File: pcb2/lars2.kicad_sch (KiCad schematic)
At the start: 1 part, among them U1 Pico

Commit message: add 3d model to prototype pcb
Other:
- title: (none) -> LARS V2
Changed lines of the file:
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@@
 	(generator_version "8.0")
 	(paper "A4")
+	(title_block
+		(title "LARS V2")
+		(date "2024-04-01")
+		(rev "1")
+		(comment 1 "https://git.xythobuz.de/thomas/drumkit")
+		(comment 2 "Licensed under the CERN-OHL-S-2.0+")
+		(comment 4 "Copyright (c) 2024 Kauzerei, Thomas Buck")
+	)
 	(symbol
 		(lib_id "KiCad-RP-Pico:Pico")

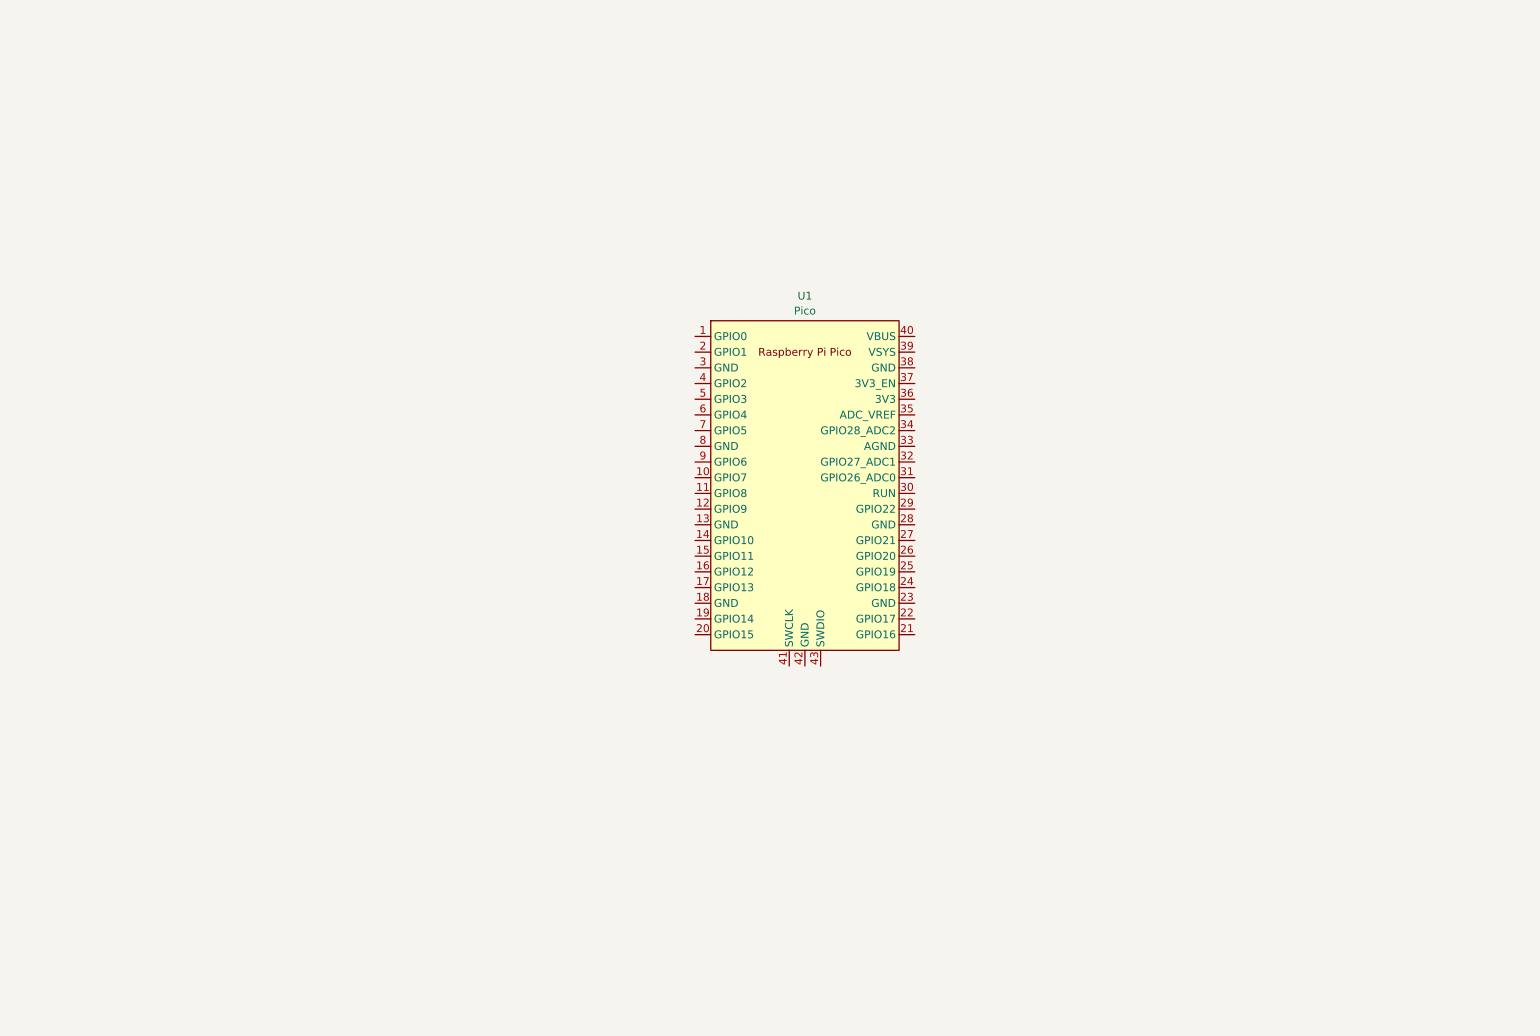
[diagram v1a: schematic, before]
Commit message: add more parts to pcb2
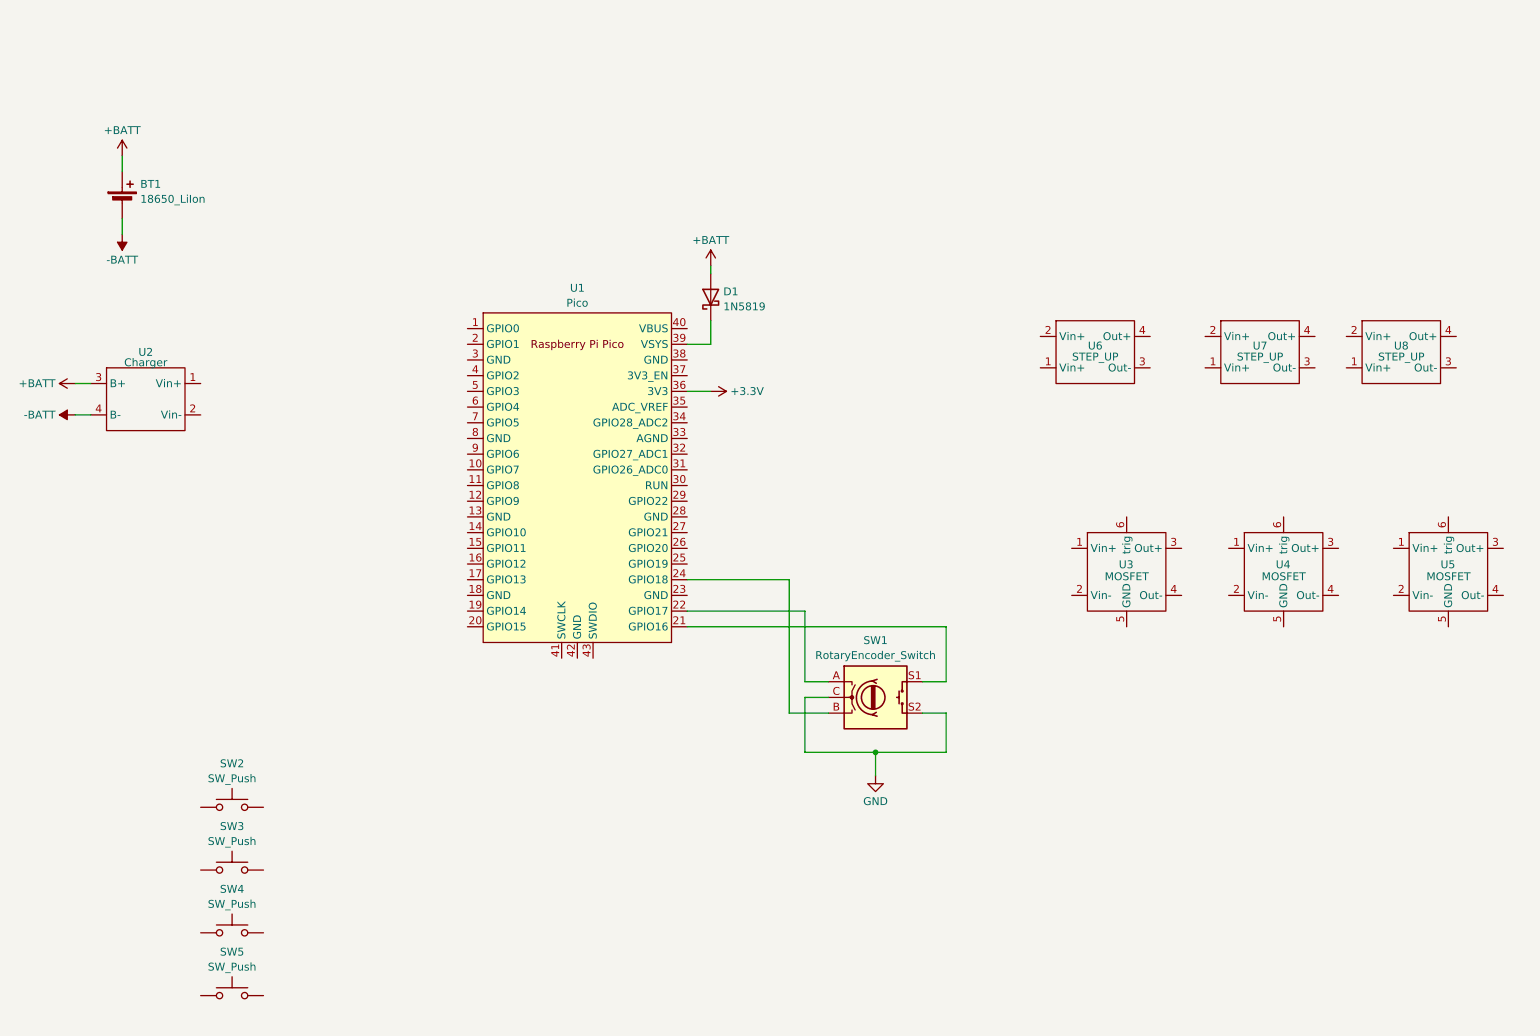
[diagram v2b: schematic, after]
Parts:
- added BT1: 18650_LiIon, Battery:BatteryHolder_Keystone_1042_1x18650, symbol Device:Battery_Cell
- added D1: 1N5819, Diode_THT:D_DO-41_SOD81_P10.16mm_Horizontal, symbol Diode:1N5819
- added SW1: RotaryEncoder_Switch, Rotary_Encoder:RotaryEncoder_Alps_EC12E-Switch_Vertical_H20mm_CircularMountingHoles, symbol Device:RotaryEncoder_Switch
- added SW2, SW3, SW4, SW5: SW_Push, Button_Switch_THT:SW_PUSH_6mm_H5mm, symbol Switch:SW_Push
- added U2: Charger, chinese_modules:charger, symbol chinese_modules:charger
- added U3, U4, U5: MOSFET, chinese_modules:xy-mos, symbol chinese_modules:xy-mos
- added U6, U7, U8: STEP_UP, chinese_modules:dc-dc module, symbol chinese_modules:dc-dc
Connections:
- net at U1.21 (GPIO16): now also SW1.S1
- net at U1.22 (GPIO17): now also SW1.A
- net at U1.24 (GPIO18): now also SW1.B
- net +3.3V: now reaches U1.36 (3V3)
- net at U1.39 (VSYS): now also D1.1 (K)
- new net +BATT: BT1.1 (+), D1.2 (A), U2.3 (B+)
- new net -BATT: BT1.2 (-), U2.4 (B-)
- new net GND: SW1.C, SW1.S2
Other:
- moved on the sheet: U1

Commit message: add more parts for pcb2 and work on placement
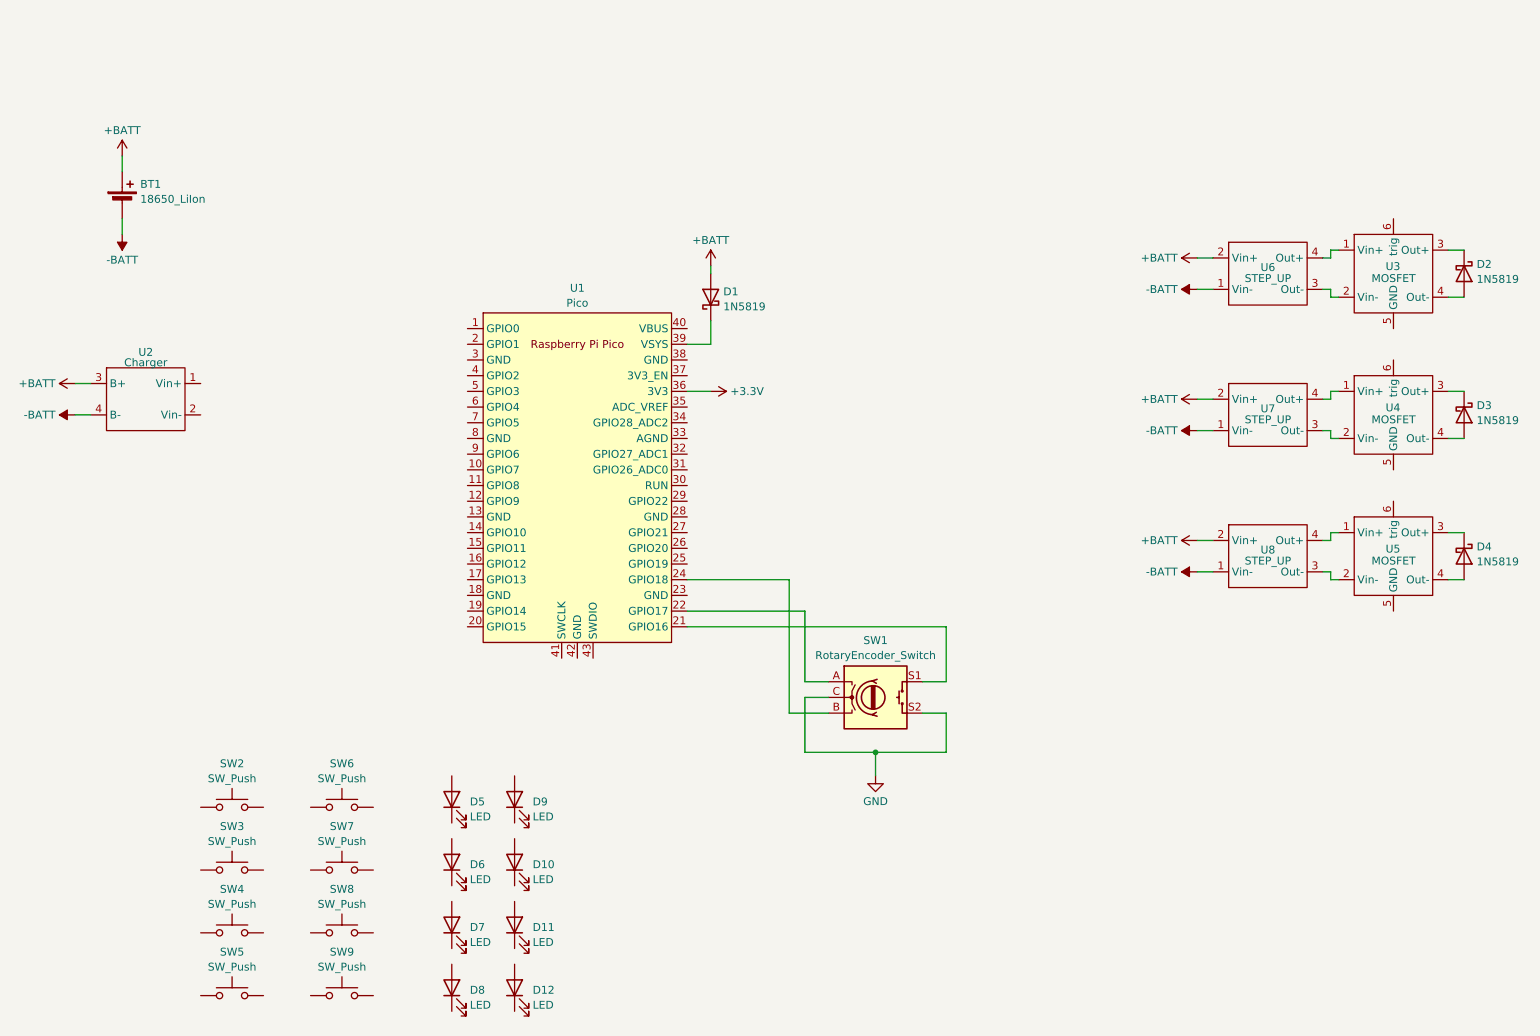
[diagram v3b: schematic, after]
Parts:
- added D10, D11, D12, D5, D6, D7, D8, D9: LED, LED_THT:LED_D5.0mm, symbol Device:LED
- added D2, D3, D4: 1N5819, Diode_THT:D_DO-41_SOD81_P10.16mm_Horizontal, symbol Diode:1N5819
- added SW6, SW7, SW8, SW9: SW_Push, Button_Switch_THT:SW_PUSH_6mm_H5mm, symbol Switch:SW_Push
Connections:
- net +BATT: now also U6.2 (Vin+), U7.2 (Vin+), U8.2 (Vin+)
- net -BATT: now also U6.1 (Vin-), U7.1 (Vin-), U8.1 (Vin-)
- net at U3.1 (Vin+): now also U6.4 (Out+)
- net at U3.2 (Vin-): now also U6.3 (Out-)
- net at U3.3 (Out+): now also D2.1 (K)
- net at U3.4 (Out-): now also D2.2 (A)
- net at U8.3 (Out-): now also U5.2 (Vin-)
- net at U8.4 (Out+): now also U5.1 (Vin+)
- net at U4.1 (Vin+): now also U7.4 (Out+)
- net at U4.2 (Vin-): now also U7.3 (Out-)
- net at U4.3 (Out+): now also D3.1 (K)
- net at U4.4 (Out-): now also D3.2 (A)
- net at U5.3 (Out+): now also D4.1 (K)
- net at U5.4 (Out-): now also D4.2 (A)
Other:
- moved on the sheet: U3, U4, U5, U6, U7, U8

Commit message: add ssd1306 oled to pcb2
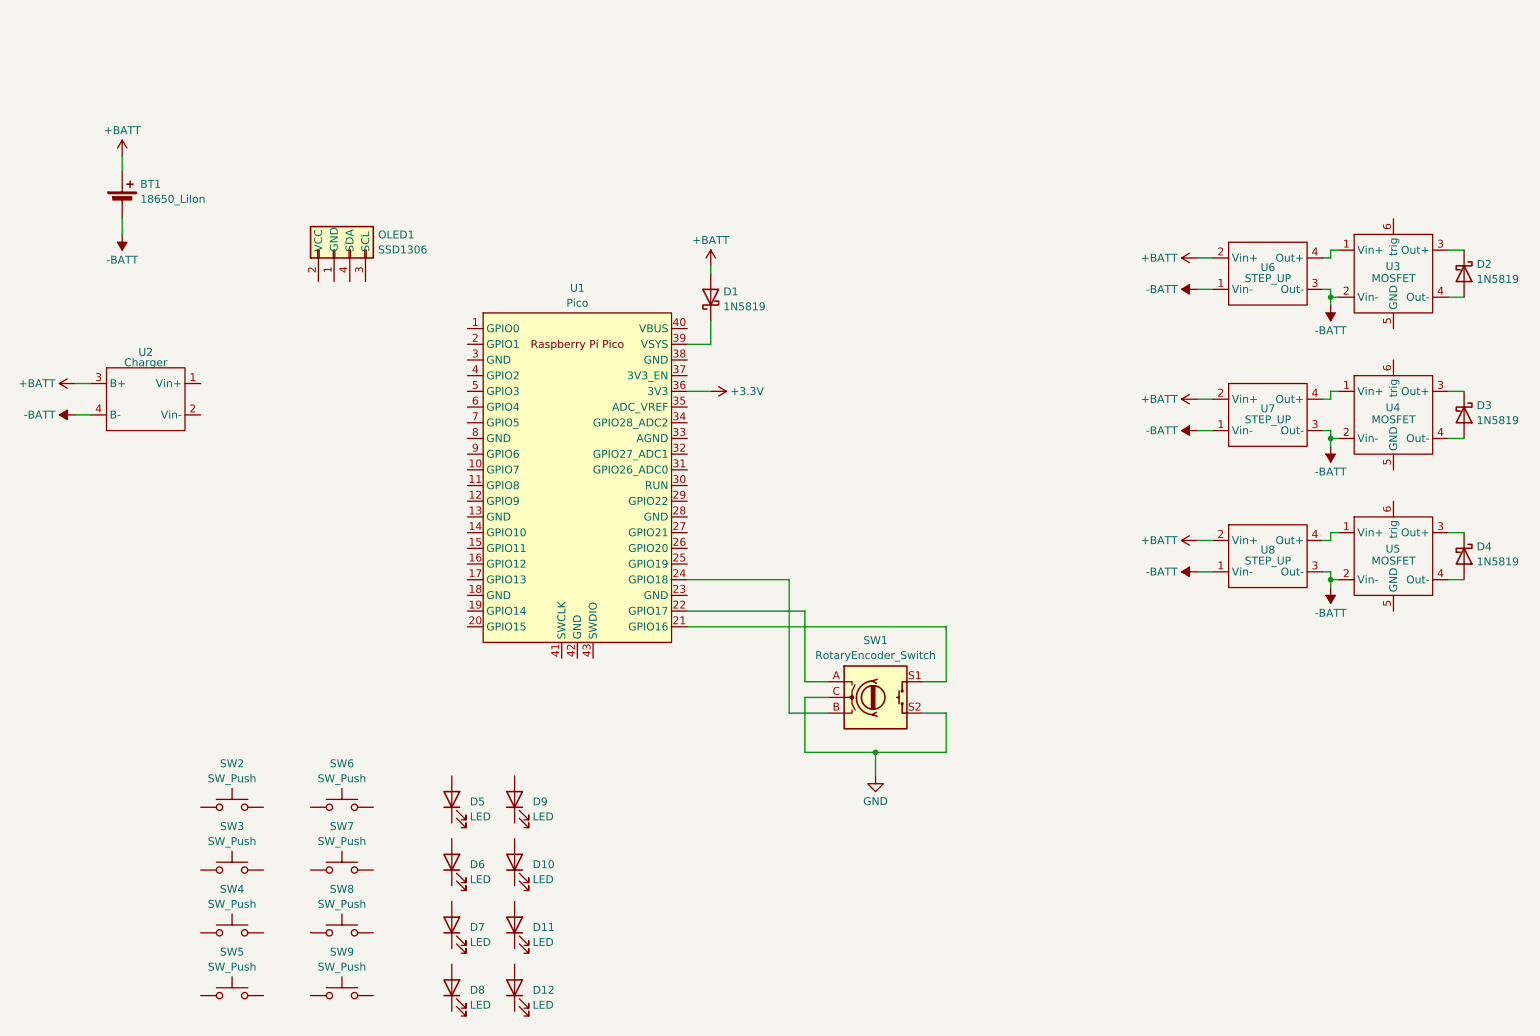
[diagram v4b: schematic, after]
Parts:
- added OLED1: SSD1306, ssd1306:SSD1306_0.96_Oled, symbol ssd1306:SSD1306
- U1: footprint MCU_RaspberryPi_and_Boards:RPi_Pico_SMD_TH -> KiCad-RP-Pico:RPi_Pico_SMD_only
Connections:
- net -BATT: now also U3.2 (Vin-), U4.2 (Vin-), U5.2 (Vin-), U6.3 (Out-), U7.3 (Out-), U8.3 (Out-)

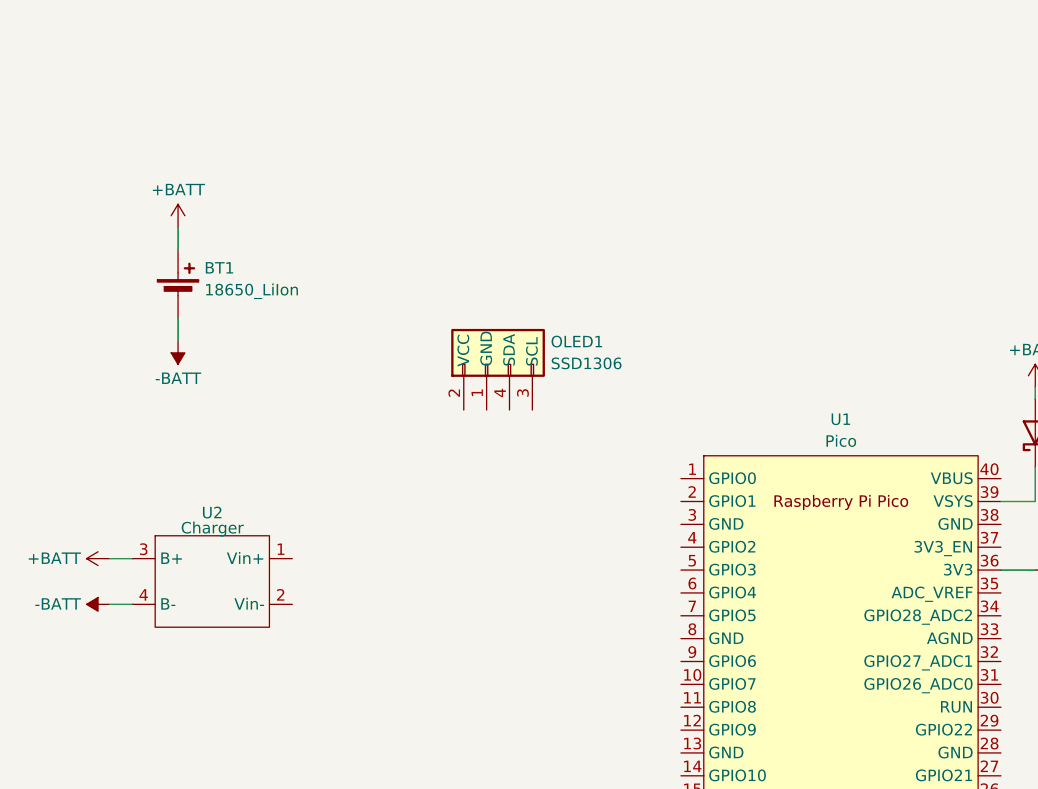
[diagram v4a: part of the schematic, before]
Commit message: add power switch and finish output routing
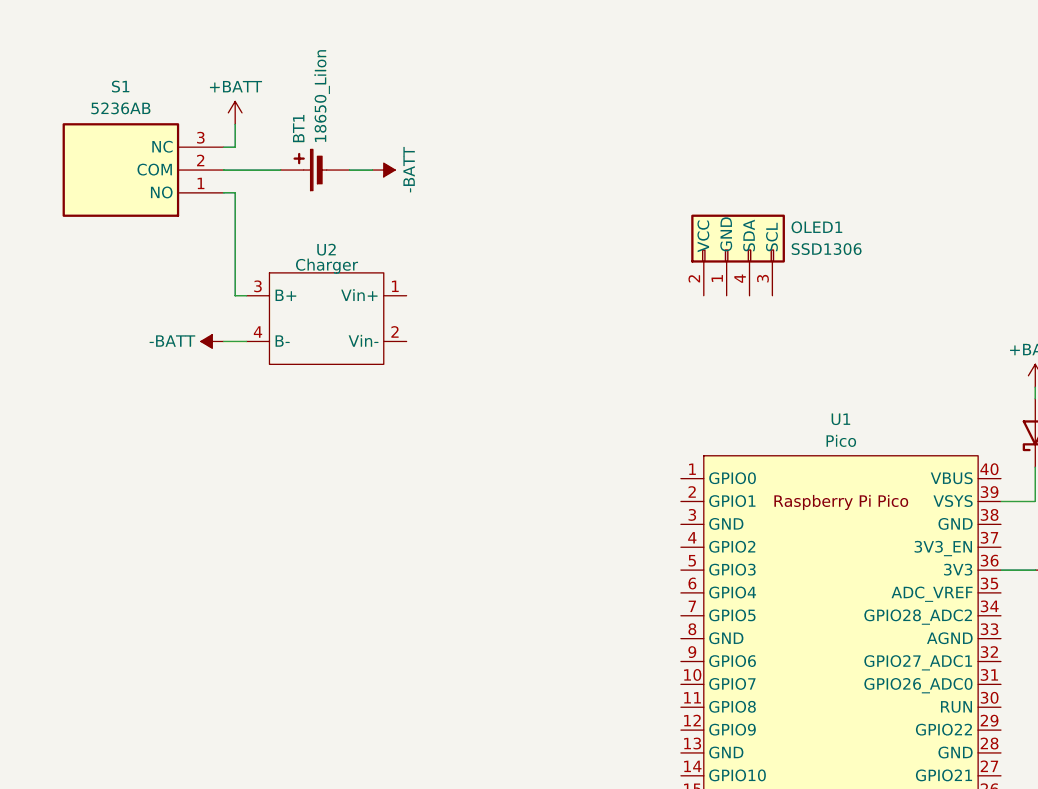
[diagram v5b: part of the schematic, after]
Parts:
- added S1: 5236AB, 5236AB, symbol 5236ab:5236AB
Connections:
- net +BATT: now also S1.3 (NC); no longer BT1.1 (+), U2.3 (B+)
- new net: S1.1 (NO), U2.3 (B+)
- new net: BT1.1 (+), S1.2 (COM)
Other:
- moved on the sheet: BT1, OLED1, U2
